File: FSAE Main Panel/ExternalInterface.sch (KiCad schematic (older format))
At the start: 40 parts, among them J201 USB Micro B, J203 Conn_01x08, J204 Conn, J3 Conn, J5 Cortex_Debug, J6 Conn, SW1 SW_SPST, SW2 SW_SPST, U201 CD40106BPWR

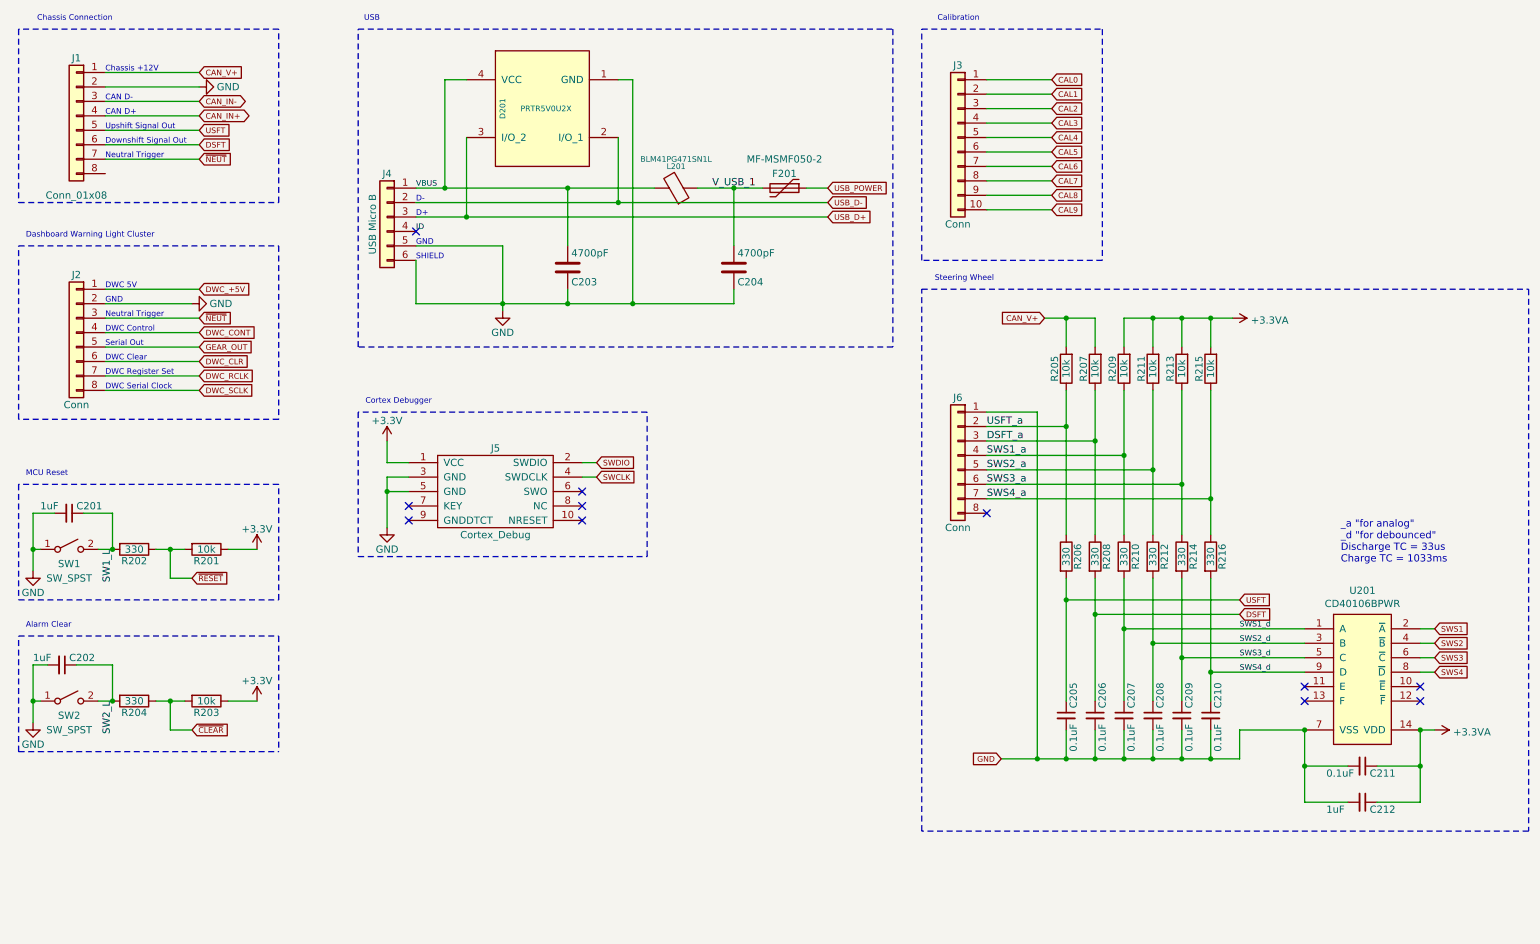
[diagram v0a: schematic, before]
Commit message: CAL Switch Input
Added Cal Switch input Decoder
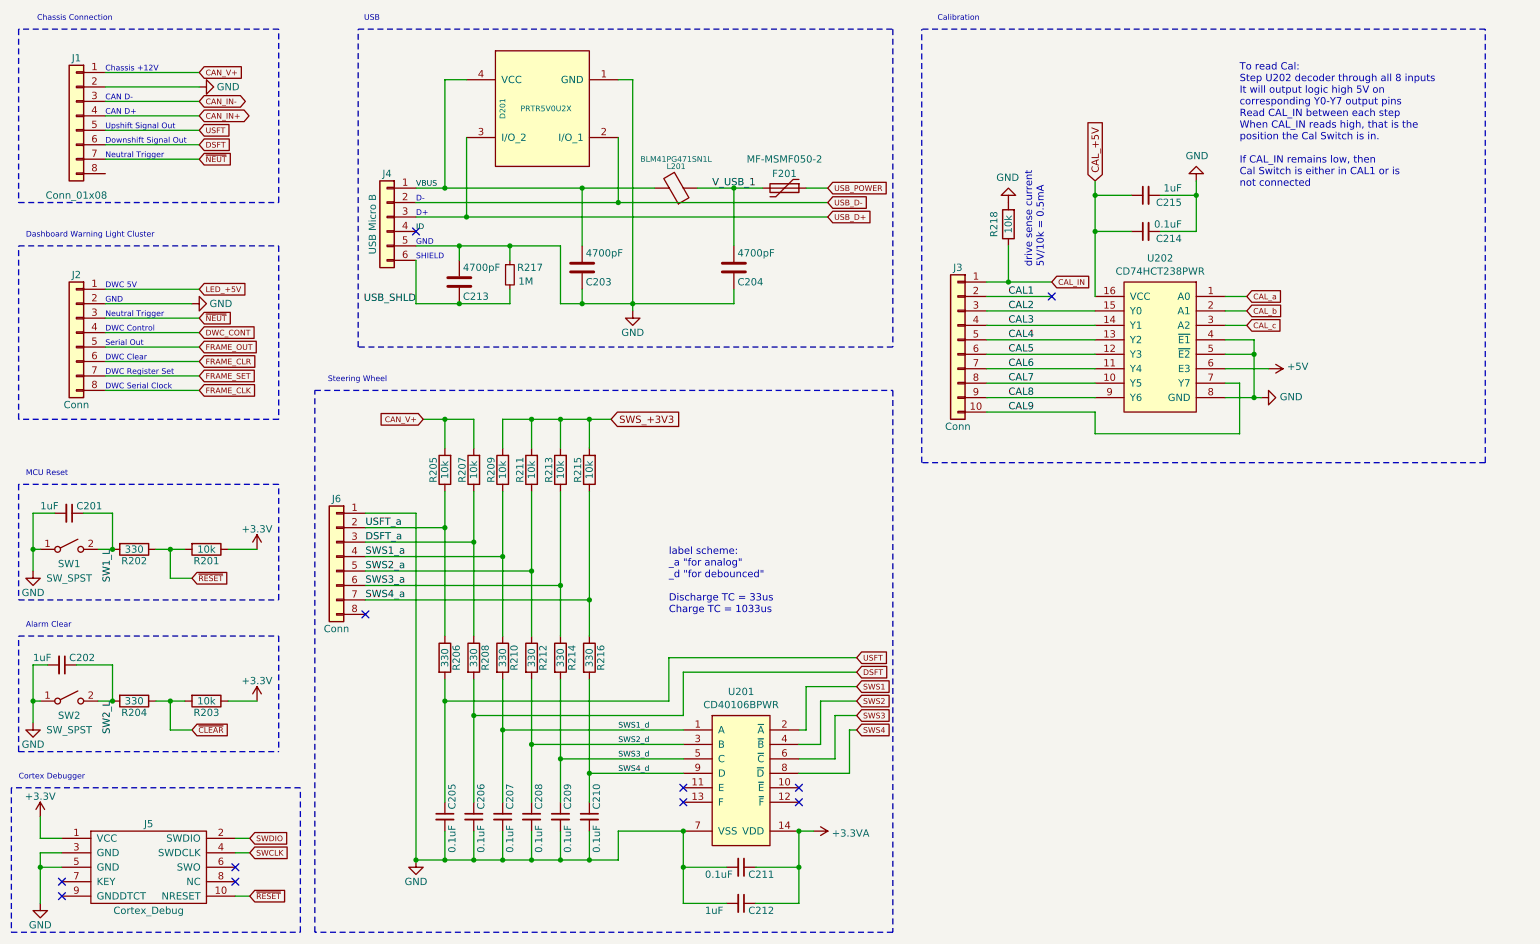
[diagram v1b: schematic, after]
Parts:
- added C213: 4700pF, Capacitors_SMD:C_0603, symbol Device:C
- added C214: 0.1uF, Capacitors_SMD:C_0603, symbol Device:C_Small
- added C215: 1uF, Capacitors_SMD:C_0603, symbol Device:C_Small
- added R217: 1M, symbol Device:R_Small
- added R218: 10k, Resistors_SMD:R_0603, symbol Device:R
- added U202: CD74HCT238PWR, Housings_SSOP:TSSOP-16_4.4x5mm_Pitch0.65mm, symbol FSAE2020:74HC238
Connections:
- net +3.3VA: no longer R209.2, R211.2, R213.2, R215.2
- net CAL2: now also U202.15 (Y0)
- net CAL3: now also U202.14 (Y1)
- net CAL4: now also U202.13 (Y2)
- net CAL5: now also U202.12 (Y3)
- net CAL6: now also U202.11 (Y4)
- net CAL7: now also U202.10 (Y5)
- net CAL8: now also U202.9 (Y6)
- net CAL9: now also U202.7 (Y7)
- net GND: now also C213.2, C214.2, C215.2, R217.1, R218.2, U202.4 (~E1), U202.5 (~E2), U202.8 (GND); no longer J201.6 (Pin_6)
- net ~RESET: now also J5.10 (NRESET)
- net CAL0 renamed CAL_IN
- net CAL_IN: now also R218.1
- net DWC_+5V renamed LED_+5V
- net DWC_CLR renamed FRAME_CLR
- net DWC_RCLK renamed FRAME_SET
- net DWC_SCLK renamed FRAME_CLK
- net GEAR_OUT renamed FRAME_OUT
- new net +5V: U202.6 (E3)
- new net CAL_+5V: C214.1, C215.1, U202.16 (VCC)
- new net CAL_a: U202.1 (A0)
- new net CAL_b: U202.2 (A1)
- new net CAL_c: U202.3 (A2)
- new net SWS_+3V3: R209.2, R211.2, R213.2, R215.2
- new net USB_SHLD: C213.1, J201.6 (Pin_6), R217.2
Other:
- note added: "To read Cal:\nStep U202 decoder through all 8 inputs\nIt will output logic high 5V on\ncorresponding Y0-Y7 output pins\nRead CAL_IN between each step\nWhen CAL_IN reads high, that is the\nposition the Cal Switch is in.\n\nIf CAL_IN remains low, then\nCal Switch is either in CAL1 or is\nnot connected"
- note added: "drive sense current\n5V/10k = 0.5mA"
- note added: "label scheme:\n_a "for analog"\n_d "for debounced"\n\nDischarge TC = 33us\nCharge TC = 1033us"
- note removed: "_a "for analog"\n_d "for debounced"\nDischarge TC = 33us\nCharge TC = 1033ms"
- moved on the sheet: C203, C205, C206, C207, C208, C209, C210, C211, C212, J3, J5, J6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

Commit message: Completed V1 of Power Section
Completed Power Section 5V and 3.3V Regulators
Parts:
- SW1, SW2: symbol Switch:SW_SPST -> Switch:SW_Push
- U202: value CD74HCT238PWR -> CD74HC238PWR
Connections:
- net +3.3VA is gone; now on net +3V3: C211.1, C212.1, U201.14 (VDD)
- net +5V is gone; now on net +3V3: U202.6 (E3)
- net SWS_+3V3 is gone; now on net EXT_+3V3: R209.2, R211.2, R213.2, R215.2
- net CAL_+5V renamed EXT_+3V3
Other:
- note added: "Calibration Switch Position Input"
- note added: "Steering Wheel Input & Passthrough"
- note added: "drive sense current\n3.3V/10k = 0.33mA"
- note removed: "Calibration"
- note removed: "Steering Wheel"
- note removed: "drive sense current\n5V/10k = 0.5mA"
- moved on the sheet: J5
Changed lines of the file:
@@
 L cortex_debug:Cortex_Debug J5
 U 1 1 5BFE970B
-P 1550 6650
-F 0 "J5" H 1550 6950 50  0000 C CNN
-F 1 "Cortex_Debug" H 1550 6350 50  0000 C CNN
-F 2 "Pin_Headers:Pin_Header_Straight_2x05_Pitch1.27mm" H 1700 6650 39  0001 C CNN
-F 3 "https://cdn.amphenol-icc.com/media/wysiwyg/files/drawing/20021111.pdf" H 1700 6650 39  0001 C CNN
-F 4 "Cortex Debug" H -2400 2900 50  0001 C CNN "Description"
-F 5 "Amphenol" H -2400 2900 50  0001 C CNN "Manufacturer"
-F 6 "20021111-00010T4LF" H -2400 2900 50  0001 C CNN "Part Number"
-	1    1550 6650
+P 7850 4650
+F 0 "J5" H 7850 4950 50  0000 C CNN
+F 1 "Cortex_Debug" H 7850 4350 50  0000 C CNN
+F 2 "Pin_Headers:Pin_Header_Straight_2x05_Pitch1.27mm" H 8000 4650 39  0001 C CNN
+F 3 "https://cdn.amphenol-icc.com/media/wysiwyg/files/drawing/20021111.pdf" H 8000 4650 39  0001 C CNN
+F 4 "Cortex Debug" H 3900 900 50  0001 C CNN "Description"
+F 5 "Amphenol" H 3900 900 50  0001 C CNN "Manufacturer"
+F 6 "20021111-00010T4LF" H 3900 900 50  0001 C CNN "Part Number"
+	1    7850 4650
 	1    0    0    -1
 $EndComp
@@
 L power:+3.3V #PWR0207
 U 1 1 5BFE98A3
-P 800 6300
-F 0 "#PWR0207" H 800 6150 50  0001 C CNN
-F 1 "+3.3V" H 800 6440 50  0000 C CNN
-F 2 "" H 800 6300 50  0001 C CNN
-F 3 "" H 800 6300 50  0001 C CNN
-	1    800  6300
+P 7100 4300
+F 0 "#PWR0207" H 7100 4150 50  0001 C CNN
+F 1 "+3.3V" H 7100 4440 50  0000 C CNN
+F 2 "" H 7100 4300 50  0001 C CNN
+F 3 "" H 7100 4300 50  0001 C CNN
+	1    7100 4300
 	1    0    0    -1
 $EndComp
@@
 L power:GND #PWR0208
 U 1 1 5BFE993E
-P 800 6900
-F 0 "#PWR0208" H 800 6650 50  0001 C CNN
-F 1 "GND" H 800 6750 50  0000 C CNN
-F 2 "" H 800 6900 50  0001 C CNN
-F 3 "" H 800 6900 50  0001 C CNN
-	1    800  6900
-	1    0    0    -1
-$EndComp
-Wire Wire Line
-	950  6450 800  6450
-Wire Wire Line
-	800  6450 800  6300
-Wire Wire Line
-	950  6550 800  6550
-Wire Wire Line
-	800  6550 800  6650
-Wire Wire Line
-	950  6650 800  6650
-Connection ~ 800  6650
-Text GLabel 2250 6450 2    39   Input ~ 0
+P 7100 4900
+F 0 "#PWR0208" H 7100 4650 50  0001 C CNN
+F 1 "GND" H 7100 4750 50  0000 C CNN
+F 2 "" H 7100 4900 50  0001 C CNN
+F 3 "" H 7100 4900 50  0001 C CNN
+	1    7100 4900
+	1    0    0    -1
+$EndComp
+Wire Wire Line
+	7250 4450 7100 4450
+Wire Wire Line
+	7100 4450 7100 4300
+Wire Wire Line
+	7250 4550 7100 4550
+Wire Wire Line
+	7100 4550 7100 4650
+Wire Wire Line
+	7250 4650 7100 4650
+Connection ~ 7100 4650
+Text GLabel 8550 4450 2    39   Input ~ 0
 SWDIO
-Text GLabel 2250 6550 2    39   Input ~ 0
+Text GLabel 8550 4550 2    39   Input ~ 0
 SWCLK
 Wire Wire Line
-	2250 6450 2150 6450
-Wire Wire Line
-	2250 6550 2150 6550
-Wire Notes Line
-	600  6100 600  7100
-Wire Notes Line
-	600  7100 2600 7100
-Wire Notes Line
-	2600 7100 2600 6100
-Wire Notes Line
-	2600 6100 600  6100
-Text Notes 650  6050 0    39   ~ 0
+	8550 4450 8450 4450
+Wire Wire Line
+	8550 4550 8450 4550
+Wire Notes Line
+	6900 4100 6900 5100
+Wire Notes Line
+	6900 5100 8900 5100
+Wire Notes Line
+	8900 5100 8900 4100
+Wire Notes Line
+	8900 4100 6900 4100
+Text Notes 6950 4050 0    39   ~ 0
 Cortex Debugger
-NoConn ~ 2150 6650
-NoConn ~ 2150 6750
-NoConn ~ 950  6750
-NoConn ~ 950  6850
+NoConn ~ 8450 4650
+NoConn ~ 8450 4750
+NoConn ~ 7250 4750
+NoConn ~ 7250 4850
 Wire Wire Line
 	1700 4450 1800 4450
@@
 	4900 2750 5600 2750
 Wire Wire Line
-	800  6650 800  6900
+	7100 4650 7100 4900
 Wire Notes Line
 	650  5850 2450 5850
@@
 Alarm Clear
 $Comp
-L Switch:SW_SPST SW2
+L Switch:SW_Push SW2
 U 1 1 5F4392E2
 P 1000 5500
@@
 $EndComp
 $Comp
-L Switch:SW_SPST SW1
+L Switch:SW_Push SW1
 U 1 1 5F43AE0A
 P 1000 4450
@@
 Text GLabel 6450 5500 2    39   Input ~ 0
 SWS2
-Text Notes 3200 3300 2    39   ~ 0
-Steering Wheel
+Text Notes 2800 3300 0    39   ~ 0
+Steering Wheel Input & Passthrough
 $Comp
 L Connector_Generic:Conn_01x08 J?
@@
 	4750 3550 4600 3550
 Connection ~ 4600 3550
-$Comp
-L power:+3.3VA #PWR?
-U 1 1 5F37B8F5
-P 6150 6400
-F 0 "#PWR?" H 6150 6250 50  0001 C CNN
-F 1 "+3.3VA" V 6165 6528 50  0000 L CNN
-F 2 "" H 6150 6400 50  0001 C CNN
-F 3 "" H 6150 6400 50  0001 C CNN
-	1    6150 6400
-	0    1    1    0
-$EndComp
 Wire Notes Line
 	6700 7100 2700 7100
@@
 Wire Notes Line
 	6700 3350 6700 7100
-Text Notes 7300 800  2    39   ~ 0
-Calibration
+Text Notes 6950 800  0    39   ~ 0
+Calibration Switch Position Input
 Wire Wire Line
 	7350 2600 7500 2600
@@
 	-1   0    0    -1
 $EndComp
-Text GLabel 2250 6850 2    39   Input ~ 0
+Text GLabel 8550 4850 2    39   Input ~ 0
 ~RESET
 Wire Wire Line
-	2250 6850 2150 6850
+	8550 4850 8450 4850
 $Comp
 L Device:C C213
@@
 Connection ~ 8800 2000
 Text Notes 7750 2500 1    50   ~ 0
-drive sense current\n5V/10k = 0.5mA
+drive sense current\n3.3V/10k = 0.33mA
 Wire Wire Line
 	8800 1900 8800 2000
@@
 P 8550 3050
 F 0 "U202" H 8550 3665 50  0000 C CNN
-F 1 "CD74HCT238PWR" H 8550 3574 50  0000 C CNN
+F 1 "CD74HC238PWR" H 8550 3574 50  0000 C CNN
 F 2 "Housings_SSOP:TSSOP-16_4.4x5mm_Pitch0.65mm" H 8550 3050 50  0001 C CNN
 F 3 "https://www.ti.com/lit/ds/symlink/cd74hc138.pdf" H 8550 3050 50  0001 C CNN
@@
 	8100 2700 8100 2250
 Connection ~ 8100 2250
-$Comp
-L power:+5V #PWR?
-U 1 1 5FD8AEE4
+Wire Wire Line
+	9300 3200 9000 3200
+Text Notes 9100 1950 0    50   ~ 0
+To read Cal:\nStep U202 decoder through all 8 inputs\nIt will output logic high 5V on\ncorresponding Y0-Y7 output pins\nRead CAL_IN between each step\nWhen CAL_IN reads high, that is the\nposition the Cal Switch is in.\n\nIf CAL_IN remains low, then\nCal Switch is either in CAL1 or is\nnot connected
+Text GLabel 4750 3550 2    39   Input ~ 0
+EXT_+3V3
+Wire Wire Line
+	5250 5600 5250 5300
+Wire Wire Line
+	5250 5300 6450 5300
+Wire Wire Line
+	3800 5600 5250 5600
+Wire Wire Line
+	6450 5200 5150 5200
+Wire Wire Line
+	5150 5200 5150 5500
+Wire Wire Line
+	3600 5500 5150 5500
+Wire Wire Line
+	6100 5700 6100 5400
+Wire Wire Line
+	6100 5400 6450 5400
+Wire Wire Line
+	6200 5800 6200 5500
+Wire Wire Line
+	6200 5500 6450 5500
+Wire Wire Line
+	6050 5800 6200 5800
+Wire Wire Line
+	6300 5900 6300 5600
+Wire Wire Line
+	6300 5600 6450 5600
+Wire Wire Line
+	6050 5900 6300 5900
+Wire Wire Line
+	6450 5700 6400 5700
+Wire Wire Line
+	6400 5700 6400 6000
+Wire Wire Line
+	6050 6000 6400 6000
+$Comp
+L power:+3.3V #PWR?
+U 1 1 5F834133
+P 6150 6400
+F 0 "#PWR?" H 6150 6250 50  0001 C CNN
+F 1 "+3.3V" V 6150 6650 50  0000 C CNN
+F 2 "" H 6150 6400 50  0001 C CNN
+F 3 "" H 6150 6400 50  0001 C CNN
+	1    6150 6400
+	0    1    1    0
+$EndComp
+$Comp
+L power:+3.3V #PWR?
+U 1 1 5F890967
 P 9300 3200
 F 0 "#PWR?" H 9300 3050 50  0001 C CNN
-F 1 "+5V" V 9315 3328 50  0000 L CNN
+F 1 "+3.3V" V 9300 3450 50  0000 C CNN
 F 2 "" H 9300 3200 50  0001 C CNN
 F 3 "" H 9300 3200 50  0001 C CNN
 	1    9300 3200
-	0    1    -1   0
-$EndComp
-Wire Wire Line
-	9300 3200 9000 3200
-Text Notes 9100 1950 0    50   ~ 0
-To read Cal:\nStep U202 decoder through all 8 inputs\nIt will output logic high 5V on\ncorresponding Y0-Y7 output pins\nRead CAL_IN between each step\nWhen CAL_IN reads high, that is the\nposition the Cal Switch is in.\n\nIf CAL_IN remains low, then\nCal Switch is either in CAL1 or is\nnot connected
-Text GLabel 8100 1900 1    50   Input ~ 0
-CAL_+5V
-Text GLabel 4750 3550 2    50   Input ~ 0
-SWS_+3V3
-Wire Wire Line
-	5250 5600 5250 5300
-Wire Wire Line
-	5250 5300 6450 5300
-Wire Wire Line
-	3800 5600 5250 5600
-Wire Wire Line
-	6450 5200 5150 5200
-Wire Wire Line
-	5150 5200 5150 5500
-Wire Wire Line
-	3600 5500 5150 5500
-Wire Wire Line
-	6100 5700 6100 5400
-Wire Wire Line
-	6100 5400 6450 5400
-Wire Wire Line
-	6200 5800 6200 5500
-Wire Wire Line
-	6200 5500 6450 5500
-Wire Wire Line
-	6050 5800 6200 5800
-Wire Wire Line
-	6300 5900 6300 5600
-Wire Wire Line
-	6300 5600 6450 5600
-Wire Wire Line
-	6050 5900 6300 5900
-Wire Wire Line
-	6450 5700 6400 5700
-Wire Wire Line
-	6400 5700 6400 6000
-Wire Wire Line
-	6050 6000 6400 6000
+	0    1    1    0
+$EndComp
+Text GLabel 8100 1900 1    39   Input ~ 0
+EXT_+3V3
 $EndSCHEMATC
